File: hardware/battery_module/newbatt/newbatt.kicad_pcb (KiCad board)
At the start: 2 copper layers, 139 x 45 mm, 32 parts, among them J1 DC050-T, J2 Conn_01x10, U1 BQ24210DQCR, U5 XC6210B332MR

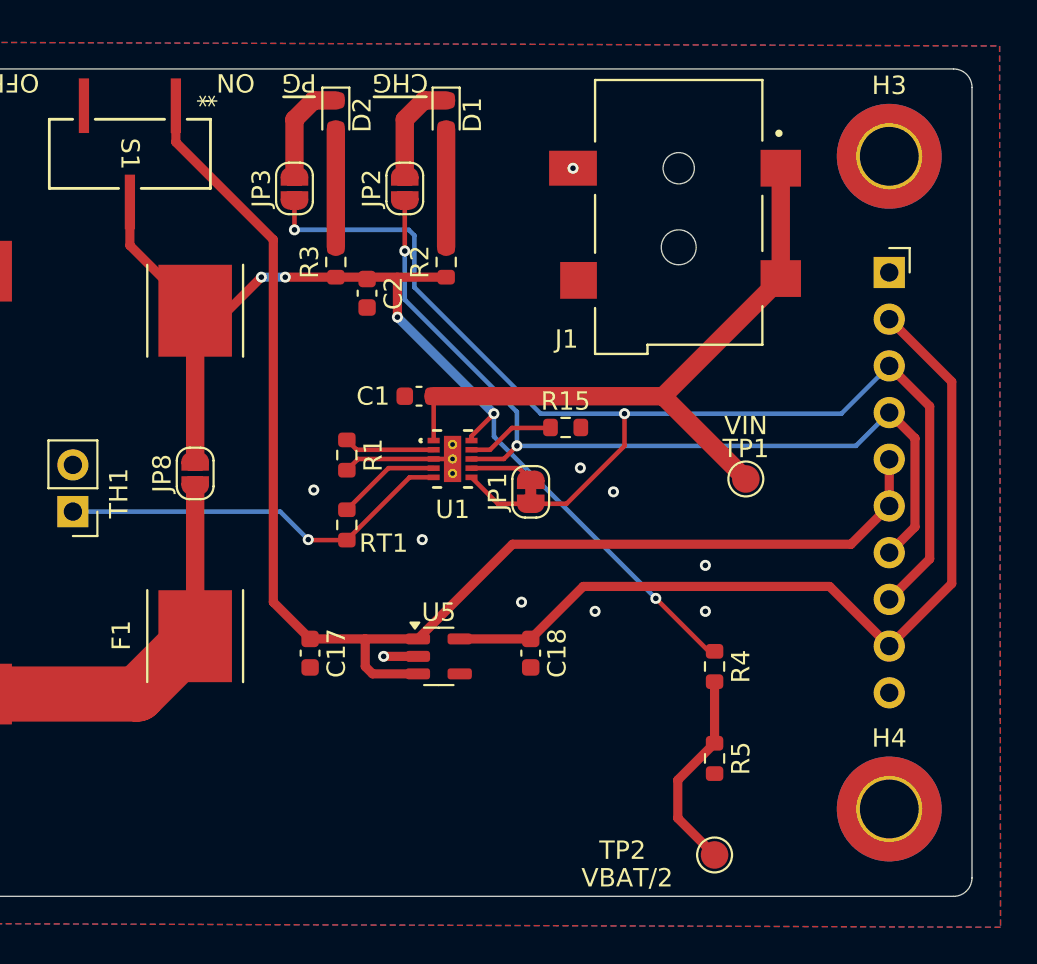
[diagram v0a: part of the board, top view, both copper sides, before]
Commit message: 1x10 pin header --> 5 pin JST
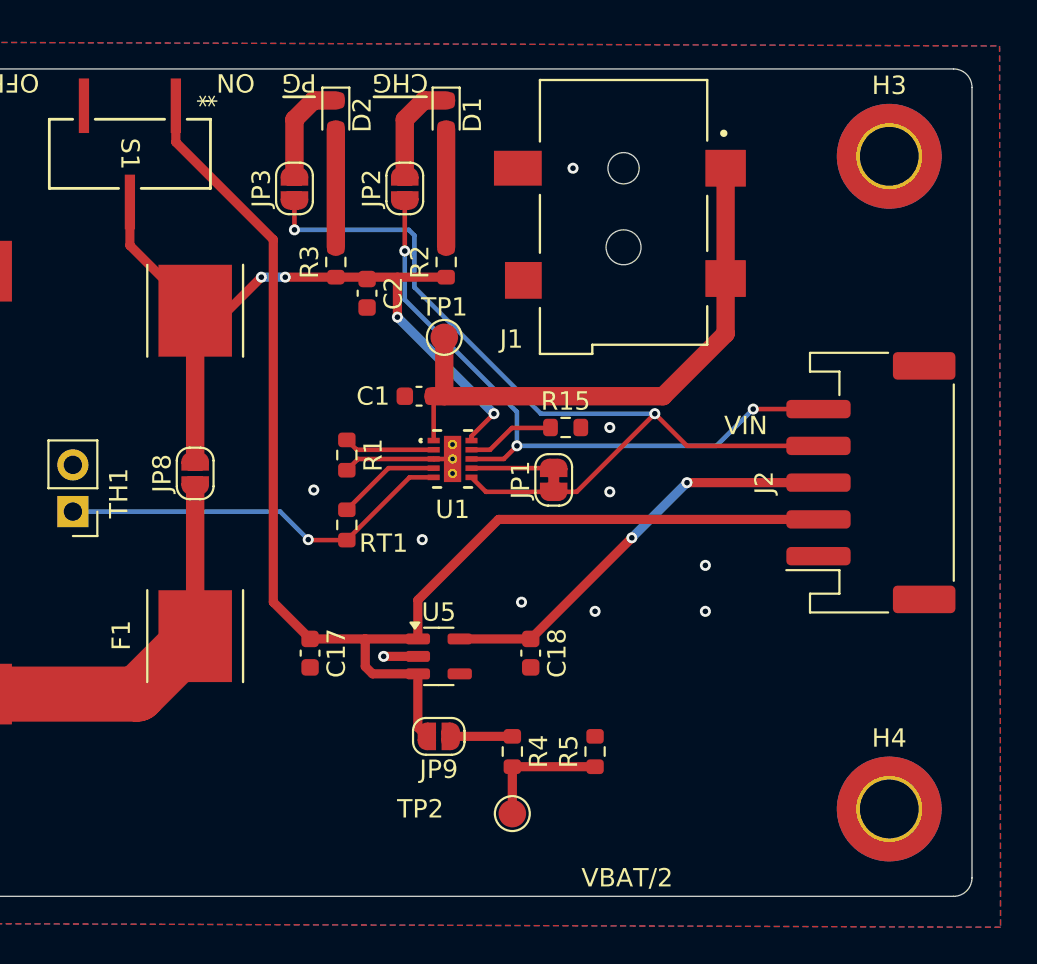
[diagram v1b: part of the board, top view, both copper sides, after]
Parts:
- added JP9: SolderJumper_2_Open, Jumper:SolderJumper-2_P1.3mm_Open_RoundedPad1.0x1.5mm, F.Cu at (125.0, 51.3)
- J2: value Conn_01x10 -> Conn_01x05_Pin; footprint Connector_PinSocket_2.54mm:PinSocket_1x10_P2.54mm_Horizontal -> Connector_JST:JST_PH_S5B-PH-SM4-TB_1x05-1MP_P2.00mm_Horizontal
- moved TP1 18.1 mm to (125.3, 29.6)
- moved R4 11.9 mm to (129.0, 52.1)
- moved J2 11.5 mm to (148.5, 37.5), turned to 90 degrees
- moved TP2 11.2 mm to (129.0, 55.5)
- moved R5 6.51 mm to (133.5, 52.1), turned to 90 degrees
- moved J1 3.00 mm to (130.5, 30.5)
- moved JP1 1.41 mm to (131.2, 37.4)
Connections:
- C17 pad 1: Net-(J2-Pin_5) -> Net-(J2-Pin_2)
- C18 pad 1: Net-(J2-Pin_2) -> Net-(J2-Pin_3)
- J2 pad 3: /~{PG} -> Net-(J2-Pin_3)
- J2 pad 4: /~{CHG} -> /~{PG}
- J2 pad 5: Net-(J2-Pin_5) -> /~{CHG}
- R4 pad 1: Net-(JP8-B) -> Net-(JP9-A)
- S1 pad 1: Net-(J2-Pin_5) -> Net-(J2-Pin_2)
- U5 pad 1: Net-(J2-Pin_5) -> Net-(J2-Pin_2)
- U5 pad 3: Net-(J2-Pin_5) -> Net-(J2-Pin_2)
- U5 pad 5: Net-(J2-Pin_2) -> Net-(J2-Pin_3)
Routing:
- net Net-(J2-Pin_5): track 73.6 -> 0.00 mm
- net Net-(J2-Pin_2): track 46.6 -> 71.7 mm
- net Net-(J2-Pin_3): track 0.00 -> 23.0 mm, vias 0 -> 2
- net /~{PG}: track 67.3 -> 48.7 mm
- net Net-(JP8-B): track 59.6 -> 41.6 mm, vias 5 -> 4
- net /~{CHG}: track 48.4 -> 35.9 mm, vias 2 -> 3
- net Net-(U1-VBUS): track 36.3 -> 31.9 mm
- net /VBAT/2: track 11.1 -> 7.05 mm
- net Net-(JP9-A): track 0.00 -> 3.35 mm
- net Net-(JP1-B): track 3.49 -> 4.18 mm

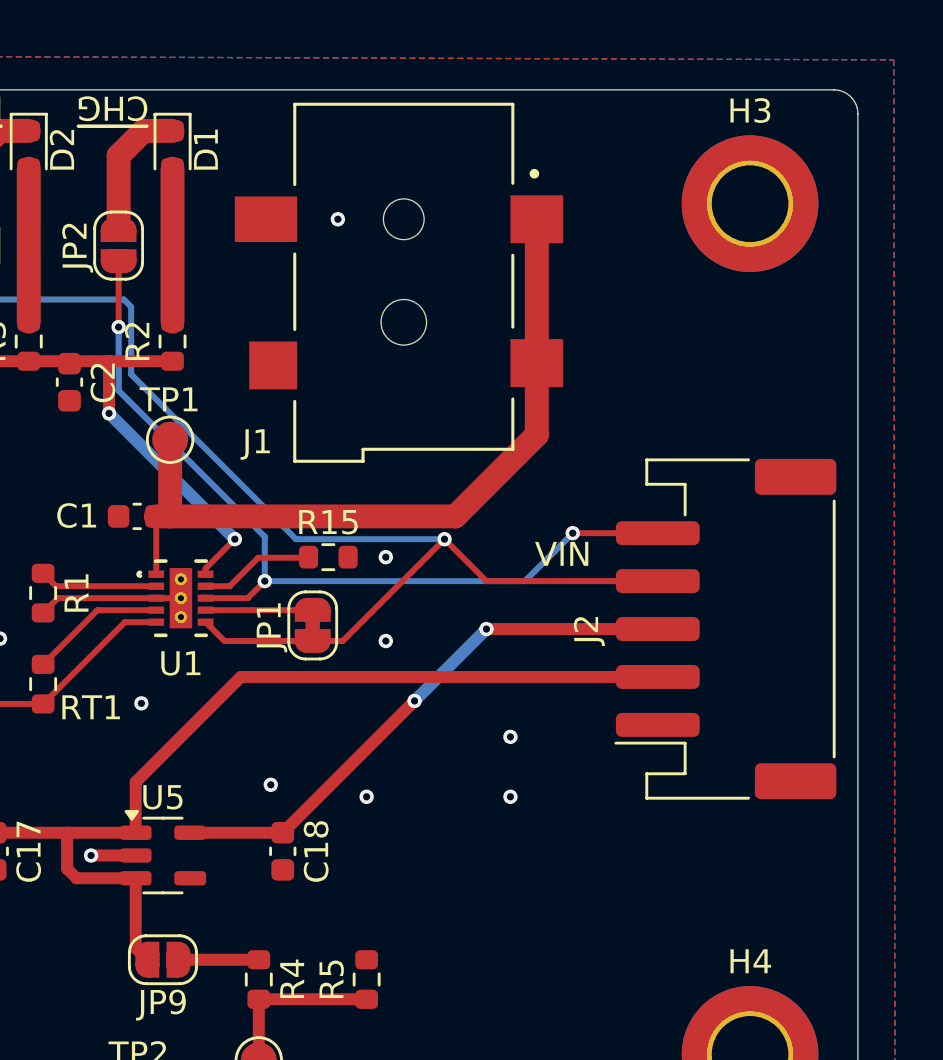
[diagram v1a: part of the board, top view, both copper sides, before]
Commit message: JST PH --> JST SH
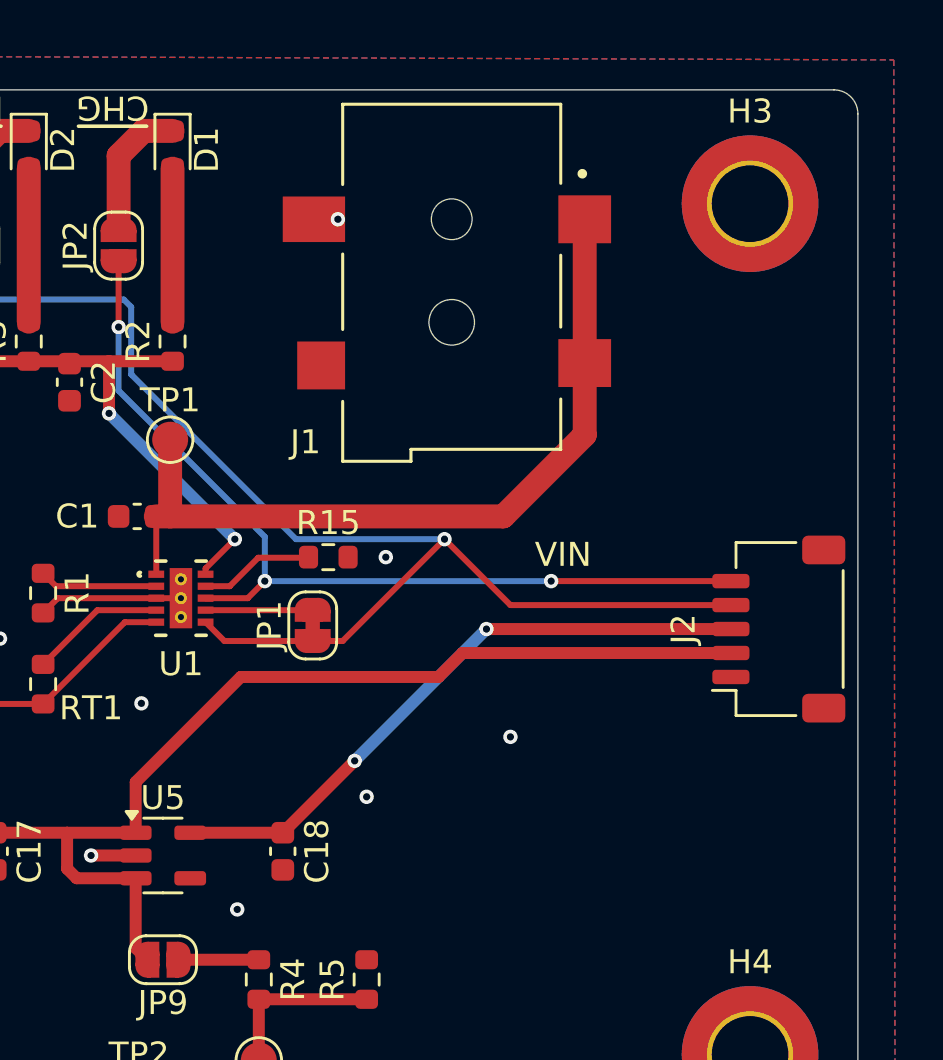
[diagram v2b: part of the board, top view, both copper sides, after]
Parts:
- J2: value Conn_01x05_Pin -> Conn_01x05_MountingPin; footprint Connector_JST:JST_PH_S5B-PH-SM4-TB_1x05-1MP_P2.00mm_Horizontal -> Connector_JST:JST_SH_SM05B-SRSS-TB_1x05-1MP_P1.00mm_Horizontal
- moved J2 2.20 mm to (150.7, 37.5)
- moved J1 2.00 mm to (132.5, 30.5)
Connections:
- J2 pad MP: (no net) -> 0
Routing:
- net /~{PG}: track 48.7 -> 52.1 mm
- net Net-(J2-Pin_2): track 71.7 -> 75.2 mm
- net Net-(J2-Pin_3): track 23.0 -> 26.1 mm
- net /~{CHG}: track 35.9 -> 38.1 mm
- net Net-(U1-VBUS): track 31.9 -> 33.9 mm
- net 0: vias 10 -> 8
